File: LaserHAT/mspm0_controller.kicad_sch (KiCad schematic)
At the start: 14 parts, among them IC1 MSPM0G3507SPTR, SW1 B, SW2 B, SW3 B, SW4 B, SW6 BSL, U5 AP2171W, U7 MSPM0G3507SRHBR

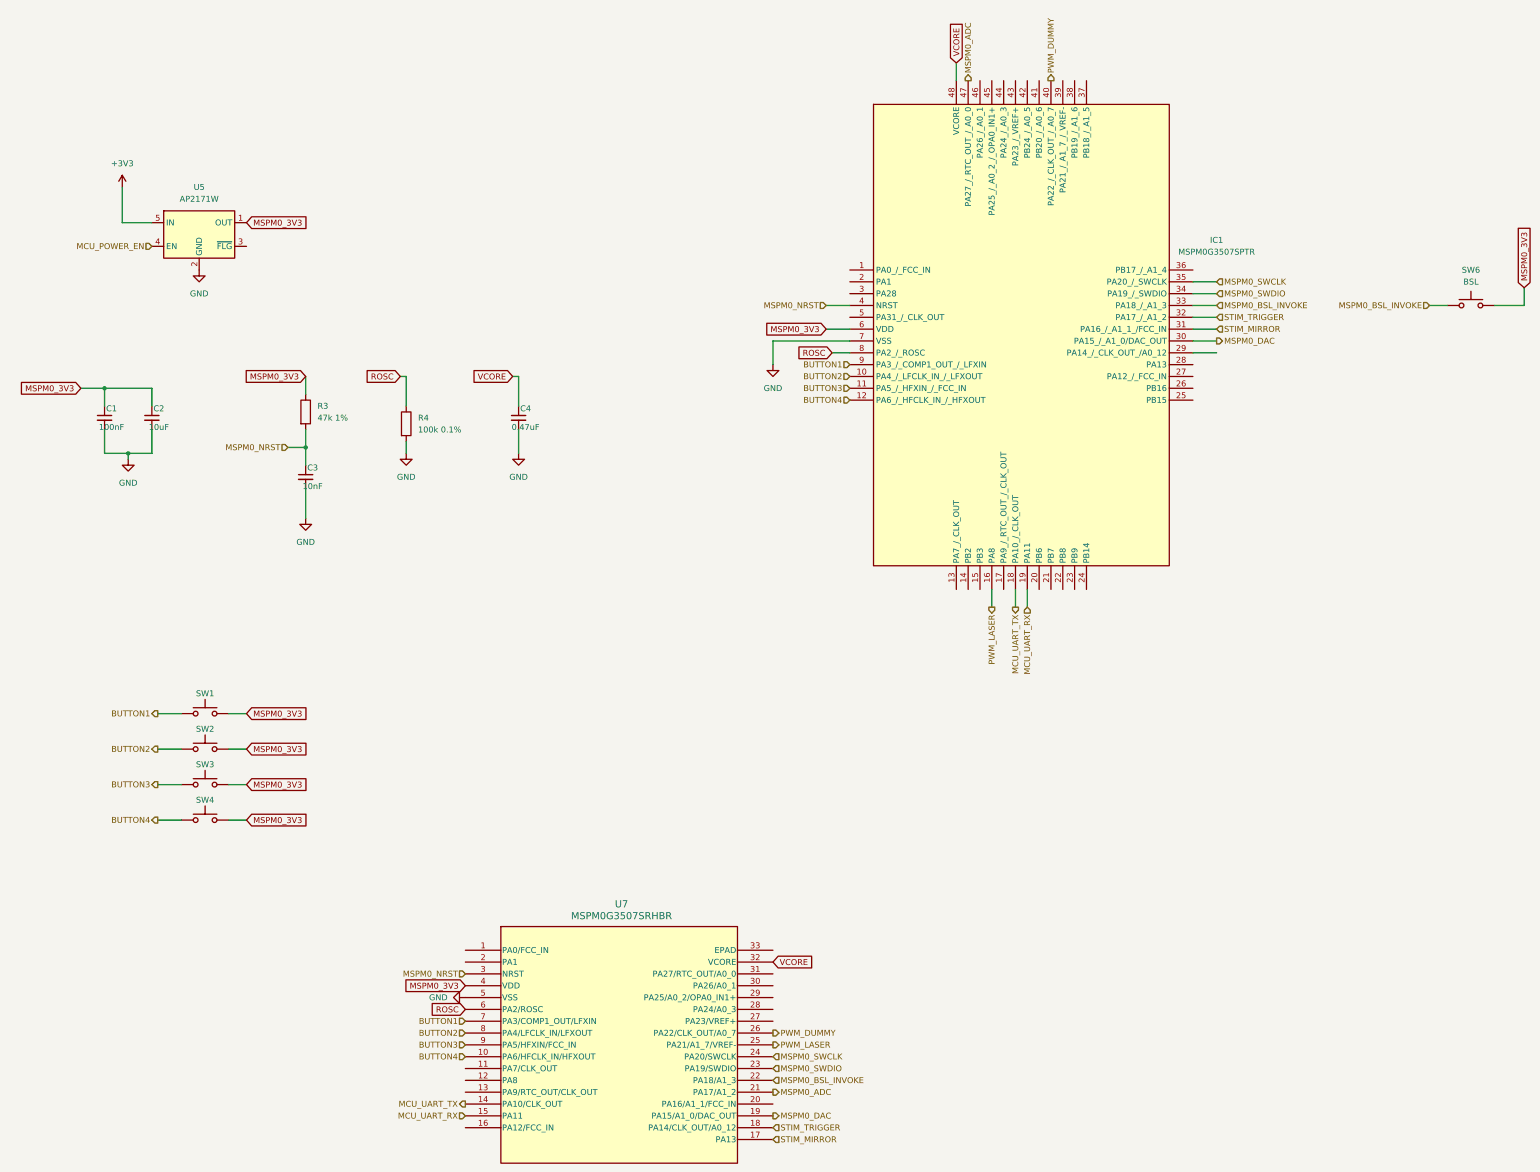
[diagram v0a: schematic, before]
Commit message: LaserHAT Rev 2: hand-routed HAT, laser + e-stim daughterboards, fab outputs
HAT (LaserHAT/):
- Rev 1 -> Rev 2 schematic migration (tools/rev2_migrate.py): issue #3 fixes,
  OLED bonnet kept, analog stage moved to plug-in daughterboards (J8/J9),
  buffered BNC I/O, USB-C power switch + PFET ideal diode.
- MCU pin map re-optimised for fewest vias: Pi UART on UART1 (PA8/PA9), I2C on
  PA0/PA1 (fail-safe), PWM_A/B on TIMA0 CCP1/CCP3 (PA7/PA12) with FAULT0 on PA6,
  active-low buttons.  Pi header: SWD swapped, NRST <-> MCU_POWER_EN swapped.
- Stable symbol UUIDs so KiCad "Update PCB" never replaces footprints.
- PCB placed and routed by hand; tidied (tools/track_tidy.py), silkscreen
  decluttered (tools/silk_declutter.py).  DRC clean apart from known cosmetic items.
- JLC fab outputs regenerated (fab/LaserHAT).
- CLAUDE.md, REV2_NOTES.md updated; portable Claude memory in claude_memory/.

Daughterboards: LaserDaughter (300 mA laser driver) and EStimDaughter (isolated
e-stim, imported from kbest/estim_module); interface spec in estim_interface/.

Firmware/Pi: `make flash HAT_REV=2` selects the Rev 2 header wiring;
Pi/power_cycle.py takes its power/reset pins from the environment.

Co-Authored-By: Claude Opus 5.5 <noreply@anthropic.com>
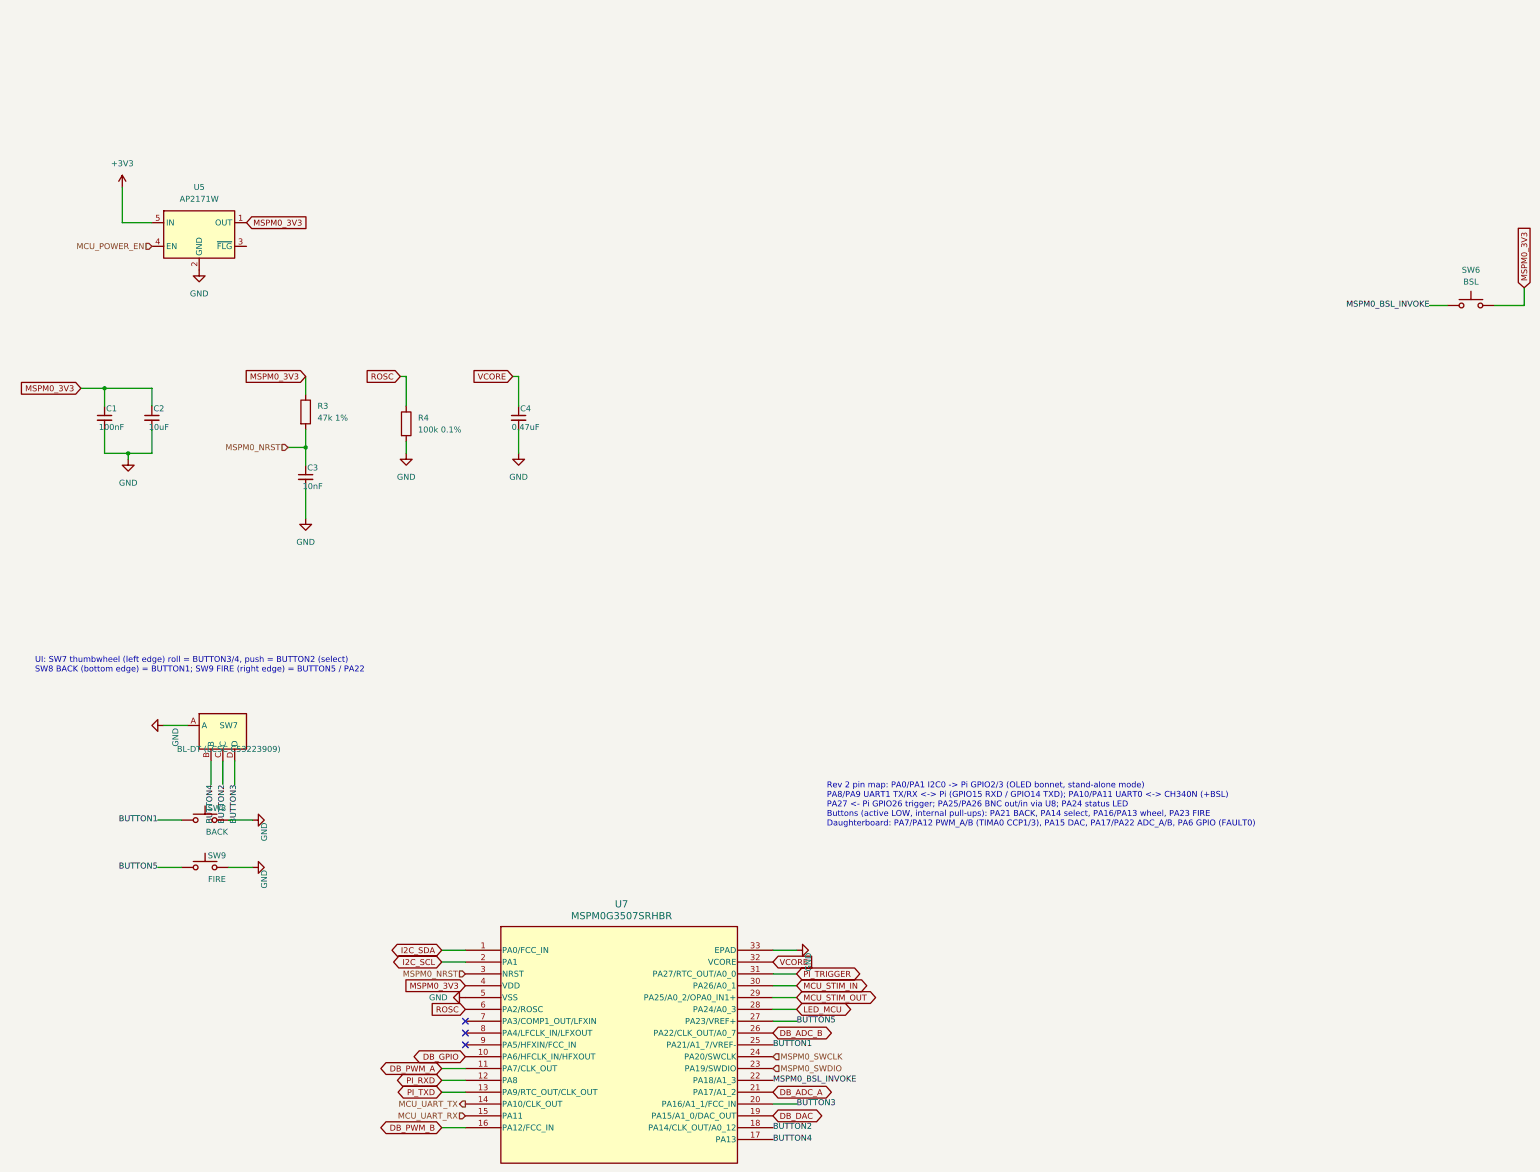
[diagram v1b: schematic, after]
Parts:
- removed IC1: MSPM0G3507SPTR, QFP50P900X900X160-48N, symbol ELEC327-Kicad:MSPM0G3507SPTR
- removed SW1, SW2, SW3, SW4: B, Button_Switch_SMD:SW_SPST_TS-1088-xR020, symbol Switch:SW_Push
- added SW7: BL-DT (LCSC C53223909), Footprints:SW-SMD_BL-DT, symbol LaserHAT:BL-DT
- added SW8: BACK, Button_Switch_THT:SW_Tactile_SPST_Angled_PTS645Vx39-2LFS, symbol Switch:SW_Push
- added SW9: FIRE, Button_Switch_SMD:SW_SPST_TS-1088-xR020, symbol Switch:SW_Push
- U7: footprint VQFN32_RHB_TEX -> ELEC327-Kicad:VQFN32_RHB_TEX
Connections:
- net PWM_LASER is gone; now on net BUTTON1: U7.25 (PA21/A1_7/VREF-)
- net STIM_MIRROR is gone; now on net BUTTON4: U7.17 (PA13)
- net STIM_TRIGGER is gone; now on net BUTTON2: U7.18 (PA14/CLK_OUT/A0_12)
- net BUTTON1: now also SW8.1; no longer U7.7 (PA3/COMP1_OUT/LFXIN)
- net BUTTON2: now also SW7.C; no longer U7.8 (PA4/LFCLK_IN/LFXOUT)
- net BUTTON3: now also U7.20 (PA16/A1_1/FCC_IN), SW7.D; no longer U7.9 (PA5/HFXIN/FCC_IN)
- net BUTTON4: now also SW7.B; no longer U7.10 (PA6/HFCLK_IN/HFXOUT)
- net GND: now also U7.33 (EPAD), SW7.A, SW8.2, SW9.2
- net I2C_SDA: now reaches U7.1 (PA0/FCC_IN)
- net DB_PWM_A: now reaches U7.11 (PA7/CLK_OUT)
- net PI_RXD: now reaches U7.12 (PA8)
- net PI_TXD: now reaches U7.13 (PA9/RTC_OUT/CLK_OUT)
- net DB_PWM_B: now reaches U7.16 (PA12/FCC_IN)
- net I2C_SCL: now reaches U7.2 (PA1)
- net BUTTON5: now reaches U7.27 (PA23/VREF+)
- net BUTTON5: now also SW9.1
- net LED_MCU: now reaches U7.28 (PA24/A0_3)
- net MCU_STIM_OUT: now reaches U7.29 (PA25/A0_2/OPA0_IN1+)
- net MCU_STIM_IN: now reaches U7.30 (PA26/A0_1)
- net PI_TRIGGER: now reaches U7.31 (PA27/RTC_OUT/A0_0)
- net MSPM0_ADC renamed DB_ADC_A
- net MSPM0_DAC renamed DB_DAC
- net PWM_DUMMY renamed DB_ADC_B
- new net DB_GPIO: U7.10 (PA6/HFCLK_IN/HFXOUT)
- no-connect marks 0 -> 3
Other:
- note added: "Rev 2 pin map: PA0/PA1 I2C0 -> Pi GPIO2/3 (OLED bonnet, stand-alone mode) PA8/PA9 UART1 TX/RX <-> Pi (GPIO15 RXD / GPIO14 TXD); PA10/PA11 UART0 <-> CH340N (+BSL) PA27 <- Pi GPIO26 trigger; PA25/PA26 BNC out/in via U8; PA24 status LED Buttons (active LOW, internal pull-ups): PA21 BACK, PA14 select, PA16/PA13 wheel, PA23 FIRE Daughterboard: PA7/PA12 PWM_A/B (TIMA0 CCP1/3), PA15 DAC, PA17/PA22 ADC_A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"
- note added: "UI: SW7 thumbwheel (left edge) roll = BUTTON3/4, push = BUTTON2 (select) SW8 BACK (bottom edge) = BUTTON1; SW9 FIRE (right edge) = BUTTON5 / PA22"
